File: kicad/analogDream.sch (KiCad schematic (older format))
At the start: 2 parts

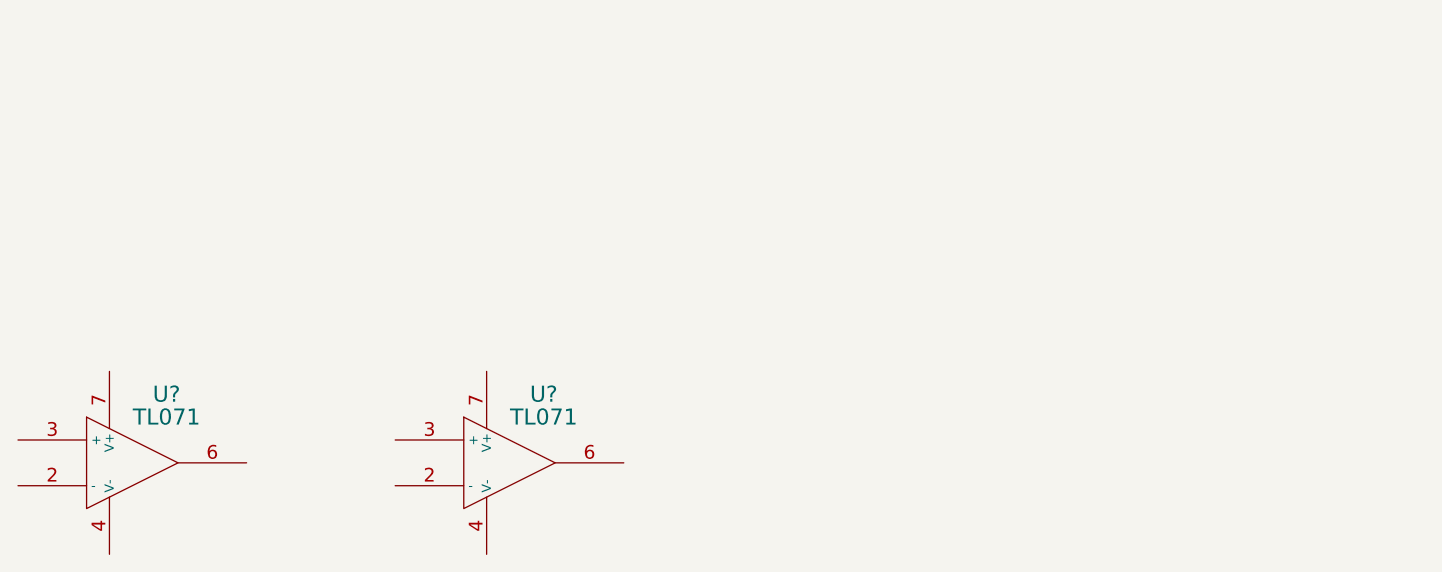
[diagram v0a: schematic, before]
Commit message: Added the base schematic for one channel
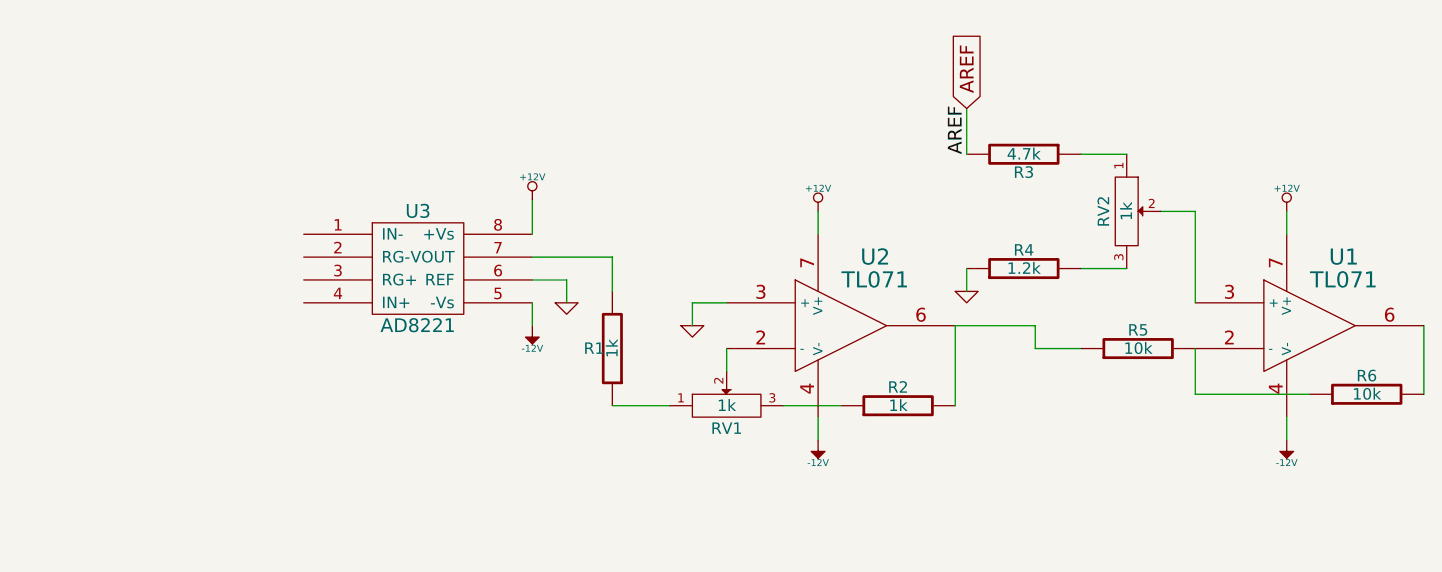
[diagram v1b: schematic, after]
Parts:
- added R1, R2: 1k, symbol R
- added R3: 4.7k, symbol R
- added R4: 1.2k, symbol R
- added R5, R6: 10k, symbol R
- added RV1, RV2: 1k, symbol POT
- added U3: AD8221, symbol AD8221
- gave numbers to parts that had none: 2
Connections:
- net at U2.2 (-): now also RV1.2
- net GND: now reaches U2.3 (+)
- net GND: now also R4.1, U3.6 (REF)
- net -12V: now reaches U2.4 (V-)
- net -12V: now also U1.4 (V-), U3.5 (-Vs)
- net at U2.6: now also R2.2, R5.1
- net +12V: now reaches U2.7 (V+)
- net +12V: now also U1.7 (V+), U3.8 (+Vs)
- net at U1.2 (-): now also R5.2, R6.1
- net at U1.3 (+): now also RV2.2
- net at U1.6: now also R6.2
- new net: R1.1, RV1.1
- new net: R1.2, U3.7 (VOUT)
- new net: R2.1, RV1.3
- new net: R3.1, RV2.1
- new net: R4.2, RV2.3
- new net AREF: R3.2
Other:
- moved on the sheet: U1, U2

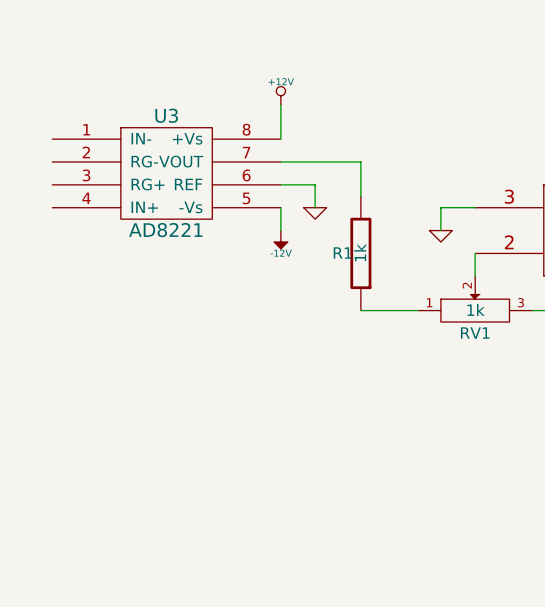
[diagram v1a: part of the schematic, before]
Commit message: Added selectable gain stage
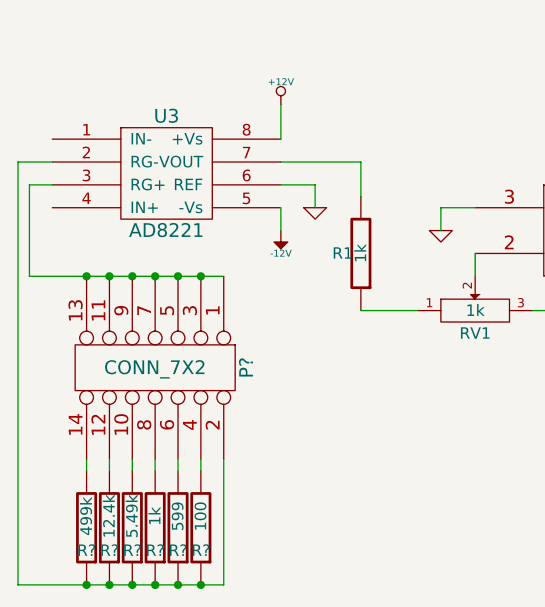
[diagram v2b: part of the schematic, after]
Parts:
- added P?: CONN_7X2, symbol CONN_7X2
- added R?: 499k, symbol R
- added R?: 12.4k, symbol R
- added R?: 5.49k, symbol R
- added R?: 1k, symbol R
- added R?: 599, symbol R
- added R?: 100, symbol R
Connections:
- net at U3.2 (RG-): now also P?.2 (P2), R?.1, R?.1, R?.1, R?.1, R?.1, R?.1
- net at U3.3 (RG+): now also P?.1 (P1), P?.11, P?.13, P?.3 (P3), P?.5 (P5), P?.7 (P7), P?.9
- new net: P?.10, R?.2
- new net: P?.12, R?.2
- new net: P?.14, R?.2
- new net: P?.4 (P4), R?.2
- new net: P?.6 (P6), R?.2
- new net: P?.8 (P8), R?.2
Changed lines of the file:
@@
-EESchema Schematic File Version 2  date Thu 24 Nov 2011 08:14:56 PM MST
+EESchema Schematic File Version 2  date Thu 24 Nov 2011 08:57:55 PM MST
 LIBS:power
 LIBS:device
@@
 LIBS:contrib
 LIBS:valves
-LIBS:ad620
-LIBS:analog-devices
-LIBS:ad8221
 LIBS:analogDream-cache
 EELAYER 24  0
@@
 Comment4 ""
 $EndDescr
+$Comp
+L R R?
+U 1 1 4ECF1235
+P 5750 3400
+F 0 "R?" H 5750 3500 50  0000 C CNN
+F 1 "100" V 5750 3350 50  0000 C CNN
+	1    5750 3400
+	-1   0    0    1
+$EndComp
+$Comp
+L R R?
+U 1 1 4ECF11D2
+P 5650 3400
+F 0 "R?" H 5650 3500 50  0000 C CNN
+F 1 "599" V 5650 3350 50  0000 C CNN
+	1    5650 3400
+	-1   0    0    1
+$EndComp
+$Comp
+L R R?
+U 1 1 4ECF1146
+P 5550 3400
+F 0 "R?" H 5550 3500 50  0000 C CNN
+F 1 "1k" V 5550 3350 50  0000 C CNN
+	1    5550 3400
+	-1   0    0    1
+$EndComp
+$Comp
+L R R?
+U 1 1 4ECF10D8
+P 5450 3400
+F 0 "R?" H 5450 3500 50  0000 C CNN
+F 1 "5.49k" V 5450 3350 50  0000 C CNN
+	1    5450 3400
+	-1   0    0    1
+$EndComp
+Connection ~ 5750 3650
+Wire Wire Line
+	5850 3650 5850 3100
+Wire Wire Line
+	5850 3650 4950 3650
+Connection ~ 5550 3650
+Connection ~ 5350 3650
+Wire Wire Line
+	4950 3650 4950 1800
+Wire Wire Line
+	4950 1800 5100 1800
+Wire Wire Line
+	5650 3150 5650 3100
+Wire Wire Line
+	5450 3150 5450 3100
+Wire Wire Line
+	5250 3150 5250 3100
+Connection ~ 5650 2300
+Connection ~ 5450 2300
+Connection ~ 5250 2300
 Wire Wire Line
 	6250 2000 6250 1900
@@
 Wire Wire Line
 	6450 1800 6100 1800
+Wire Wire Line
+	5100 1900 5000 1900
+Wire Wire Line
+	5000 1900 5000 2300
+Connection ~ 5350 2300
+Connection ~ 5550 2300
+Wire Wire Line
+	5000 2300 5850 2300
+Connection ~ 5750 2300
+Wire Wire Line
+	5350 3150 5350 3100
+Wire Wire Line
+	5550 3150 5550 3100
+Wire Wire Line
+	5750 3150 5750 3100
+Connection ~ 5250 3650
+Connection ~ 5450 3650
+Connection ~ 5650 3650
+$Comp
+L R R?
+U 1 1 4ECF0EF7
+P 5350 3400
+F 0 "R?" H 5350 3500 50  0000 C CNN
+F 1 "12.4k" V 5350 3350 50  0000 C CNN
+	1    5350 3400
+	-1   0    0    1
+$EndComp
+$Comp
+L R R?
+U 1 1 4ECF0EEF
+P 5250 3400
+F 0 "R?" H 5250 3500 50  0000 C CNN
+F 1 "499k" V 5250 3350 50  0000 C CNN
+	1    5250 3400
+	-1   0    0    1
+$EndComp
+$Comp
+L CONN_7X2 P?
+U 1 1 4ECF0EB2
+P 5550 2700
+F 0 "P?" H 5550 3100 60  0000 C CNN
+F 1 "CONN_7X2" V 5550 2700 60  0000 C CNN
+	1    5550 2700
+	0    1    1    0
+$EndComp
 $Comp
 L GND #PWR01

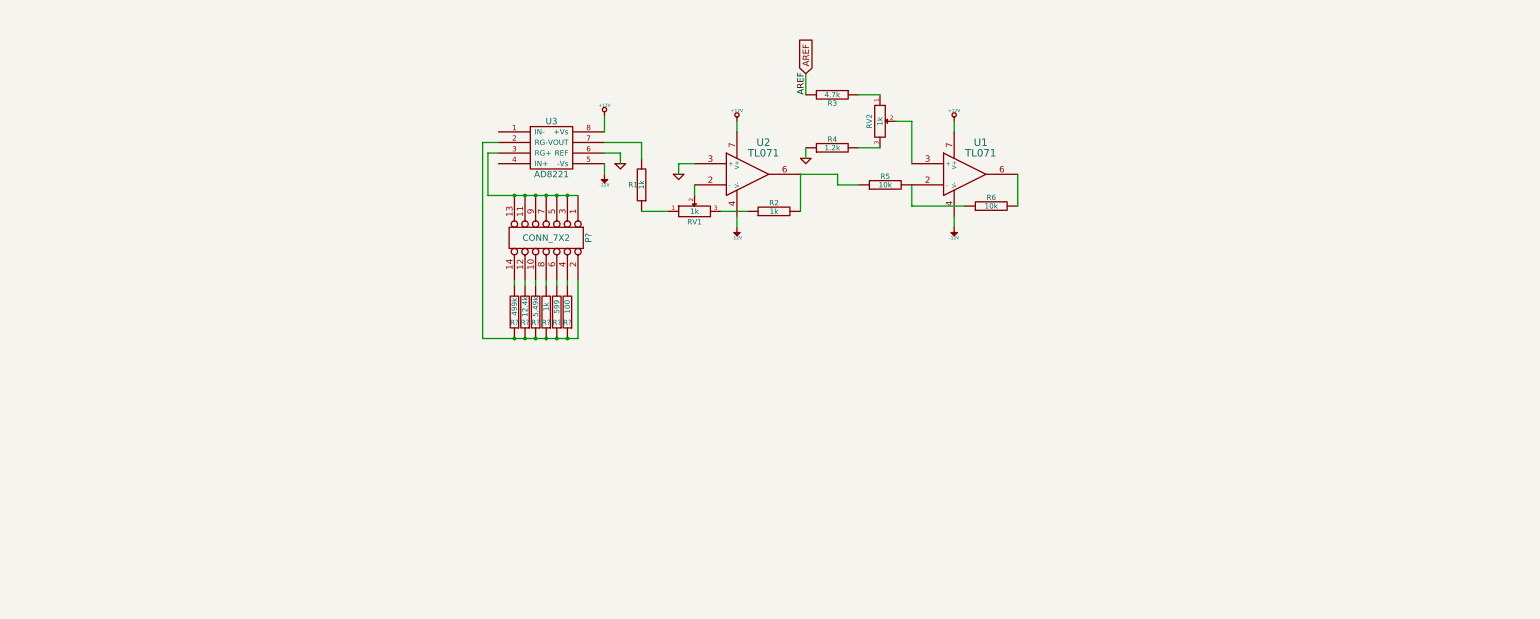
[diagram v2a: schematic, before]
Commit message: Have all 4 channels with gain and attenuation selection
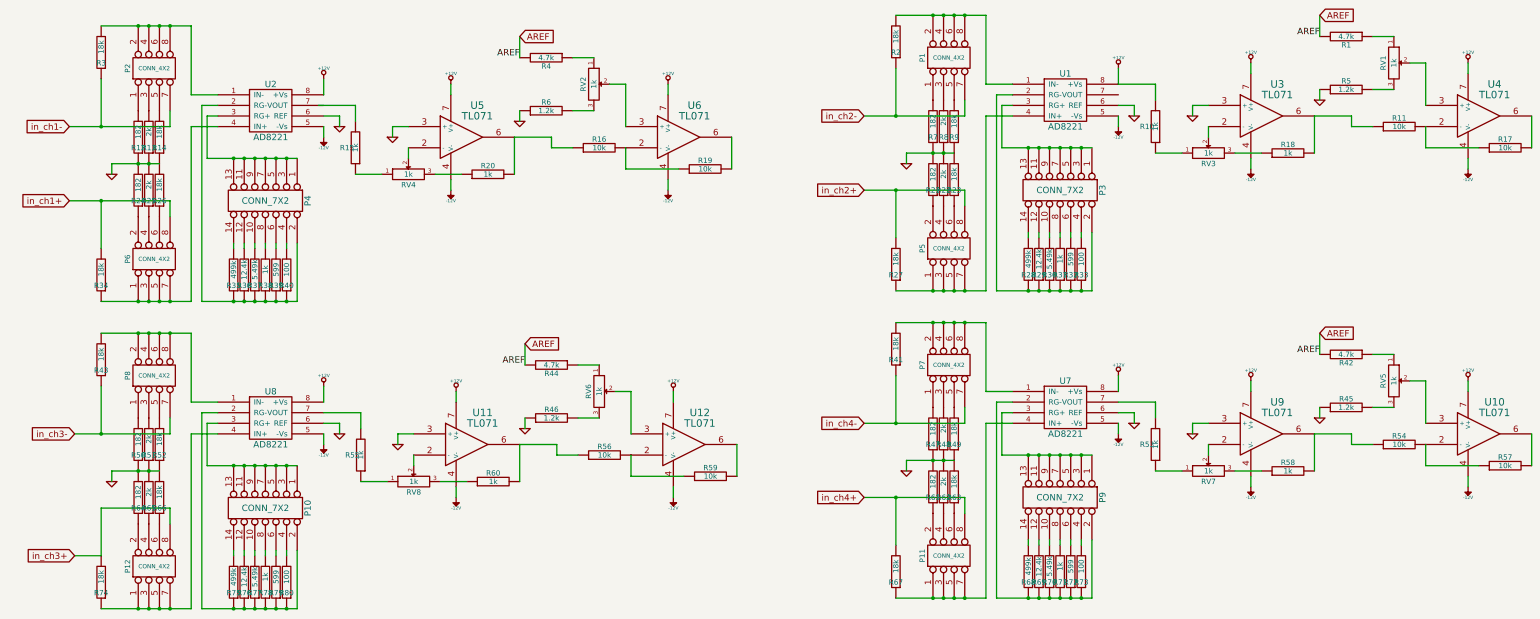
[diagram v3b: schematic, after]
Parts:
- added P1, P11, P12, P2, P5, P6, P7, P8: CONN_4X2, symbol CONN_4X2
- added P10, P3, P9: CONN_7X2, symbol CONN_7X2
- added R1, R42, R44: 4.7k, symbol R
- added R10, R18, R31, R53, R55, R58, R60, R71, R78: 1k, symbol R
- added R11, R17, R54, R56, R57, R59: 10k, symbol R
- added R12, R21, R24, R47, R50, R61, R64, R7: 182, symbol R
- added R13, R22, R25, R48, R51, R62, R65, R8: 2k, symbol R
- added R14, R2, R23, R26, R27, R3, R34, R41, R43, R49, R52, R63, R66, R67, R74, R9: 18k, symbol R
- added R28, R68, R75: 499k, symbol R
- added R29, R69, R76: 12.4k, symbol R
- added R30, R70, R77: 5.49k, symbol R
- added R32, R72, R79: 599, symbol R
- added R33, R73, R80: 100, symbol R
- added R45, R46, R5: 1.2k, symbol R
- added RV1, RV3, RV5, RV6, RV7, RV8: 1k, symbol POT
- added U1, U7, U8: AD8221, symbol AD8221
- added U10, U11, U12, U3, U4, U9: TL071, symbol TL071
- gave numbers to parts that had none: 7
- renumbered R1 to R15, R5 to R16, R6 to R19, R2 to R20, R3 to R4, R4 to R6, RV1 to RV4, U3 to U2, U2 to U5, U1 to U6
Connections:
- net +12V: now also R10.2, U1.8 (+Vs), U10.7 (V+), U11.7 (V+), U12.7 (V+), U3.7 (V+), U4.7 (V+), U7.8 (+Vs), U8.8 (+Vs), U9.7 (V+)
- net -12V: now also U1.5 (-Vs), U10.4 (V-), U11.4 (V-), U12.4 (V-), U3.4 (V-), U4.4 (V-), U7.5 (-Vs), U8.5 (-Vs), U9.4 (V-)
- net AREF: now also R1.2, R42.2, R44.2
- net GND: now also R12.1, R13.1, R14.1, R21.2, R22.2, R23.2, R24.2, R25.2, R26.2, R45.1, R46.1, R47.1, R48.1, R49.1, R5.1, R50.1, R51.1, R52.1, R61.2, R62.2, R63.2, R64.2, R65.2, R66.2, R7.1, R8.1, R9.1, U1.6 (REF), U11.3 (+), U3.3 (+), U7.6 (REF), U8.6 (REF), U9.3 (+)
- net at R15.2: no longer U2.7 (VOUT)
- net at U2.1 (IN-): now also P2.2, P2.4, P2.6, P2.8, R3.2
- net at U2.4 (IN+): now also P6.1, P6.3, P6.5, P6.7, R34.1
- new net: P2.1, R12.2
- new net: P2.3, R13.2
- new net: P2.5, R14.2
- new net: P6.2, R24.1
- new net: P6.4, R25.1
- new net: P6.6, R26.1
- new net: P12.1, P12.3, P12.5, P12.7, R74.1, U8.4 (IN+)
- new net: P8.2, P8.4, P8.6, P8.8, R43.2, U8.1 (IN-)
- new net: P8.1, R50.2
- new net: P12.2, R64.1
- new net: P8.3, R51.2
- new net: P12.4, R65.1
- new net: P12.6, R66.1
- new net: P8.5, R52.2
- new net: P10.2 (P2), R75.1, R76.1, R77.1, R78.1, R79.1, R80.1, U8.2 (RG-)
- new net: P10.4 (P4), R80.2
- new net: P10.6 (P6), R79.2
- new net: P10.8 (P8), R78.2
- new net: P10.10, R77.2
- new net: P10.12, R76.2
- new net: P10.14, R75.2
- new net: P10.1 (P1), P10.11, P10.13, P10.3 (P3), P10.5 (P5), P10.7 (P7), P10.9, U8.3 (RG+)
- new net: R55.2, U8.7 (VOUT)
- new net: R44.1, RV6.1
- new net: R46.2, RV6.3
- new net: RV6.2, U12.3 (+)
- new net: R56.2, R59.1, U12.2 (-)
- new net: R59.2, U12.6
- new net: R56.1, R60.2, U11.6
- new net: R60.1, RV8.3
- new net: R55.1, RV8.1
- new net: RV8.2, U11.2 (-)
- new net: P1.2, P1.4, P1.6, P1.8, R2.2, U1.1 (IN-)
- new net: P3.2 (P2), R28.1, R29.1, R30.1, R31.1, R32.1, R33.1, U1.2 (RG-)
- new net: P3.1 (P1), P3.11, P3.13, P3.3 (P3), P3.5 (P5), P3.7 (P7), P3.9, U1.3 (RG+)
- new net: P5.1, P5.3, P5.5, P5.7, R27.1, U1.4 (IN+)
- new net: P3.10, R30.2
- new net: P3.12, R29.2
- new net: P3.14, R28.2
- new net: P3.4 (P4), R33.2
- new net: P3.6 (P6), R32.2
- new net: P3.8 (P8), R31.2
- new net: P1.1, R7.2
- new net: P1.3, R8.2
- new net: P1.5, R9.2
- new net: P5.2, R21.1
- new net: P5.4, R22.1
- new net: P5.6, R23.1
- new net: P7.2, P7.4, P7.6, P7.8, R41.2, U7.1 (IN-)
- new net: P9.2 (P2), R68.1, R69.1, R70.1, R71.1, R72.1, R73.1, U7.2 (RG-)
- new net: P9.1 (P1), P9.11, P9.13, P9.3 (P3), P9.5 (P5), P9.7 (P7), P9.9, U7.3 (RG+)
- new net: P11.1, P11.3, P11.5, P11.7, R67.1, U7.4 (IN+)
- new net: R53.2, U7.7 (VOUT)
- new net: P9.10, R70.2
- new net: P9.12, R69.2
- new net: P9.14, R68.2
- new net: P9.4 (P4), R73.2
- new net: P9.6 (P6), R72.2
- new net: P9.8 (P8), R71.2
- new net: P7.1, R47.2
- new net: P7.3, R48.2
- new net: P7.5, R49.2
- new net: P11.2, R61.1
- new net: P11.4, R62.1
- new net: P11.6, R63.1
- new net: RV3.2, U3.2 (-)
- new net: R11.1, R18.2, U3.6
- new net: R11.2, R17.1, U4.2 (-)
- new net: RV1.2, U4.3 (+)
- new net: R17.2, U4.6
- new net: R10.1, RV3.1
- new net: R18.1, RV3.3
- new net: R1.1, RV1.1
- new net: R5.2, RV1.3
- new net: RV7.2, U9.2 (-)
- new net: R54.1, R58.2, U9.6
- new net: R54.2, R57.1, U10.2 (-)
- new net: RV5.2, U10.3 (+)
- new net: R57.2, U10.6
- new net: R53.1, RV7.1
- new net: R58.1, RV7.3
- new net: R42.1, RV5.1
- new net: R45.2, RV5.3
- new net in_ch1+: P6.8, R34.2
- new net in_ch1-: P2.7, R3.1
- new net in_ch2+: P5.8, R27.2
- new net in_ch2-: P1.7, R2.1
- new net in_ch3+: P12.8, R74.2
- new net in_ch3-: P8.7, R43.1
- new net in_ch4+: P11.8, R67.2
- new net in_ch4-: P7.7, R41.1
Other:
- moved on the sheet: P4, R15, R16, R19, R20, R35, R36, R37, R38, R39, R4, R40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
